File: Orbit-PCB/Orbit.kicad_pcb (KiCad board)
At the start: 2 copper layers, 303.2 x 145.3 mm, 287 parts, among them J1 PJ-3200B-4A, J10 Breakaway_Tabs, J11 PJ-3200B-4A, J12 AVR-ISP-6, J13 Breakaway_Tabs, J14 Breakaway_Tabs, J17 Breakaway_Tabs, J18 Breakaway_Tabs, J19 Breakaway_Tabs, J2 AVR-ISP-6, J20 Breakaway_Tabs, J3 Breakaway_Tabs, J5 Breakaway_Tabs, J6 Breakaway_Tabs, J7 Breakaway_Tabs, J9 Breakaway_Tabs, Q1 2N7002, Q2 2N7002, SW1 SW_Push, SW2 SW_Push, U1 ATmega32U4-MU, U2 PRTR5V0U2X, U3 ATmega32U4-MU, U4 PRTR5V0U2X, Y1 16MHz, Y2 16MHz

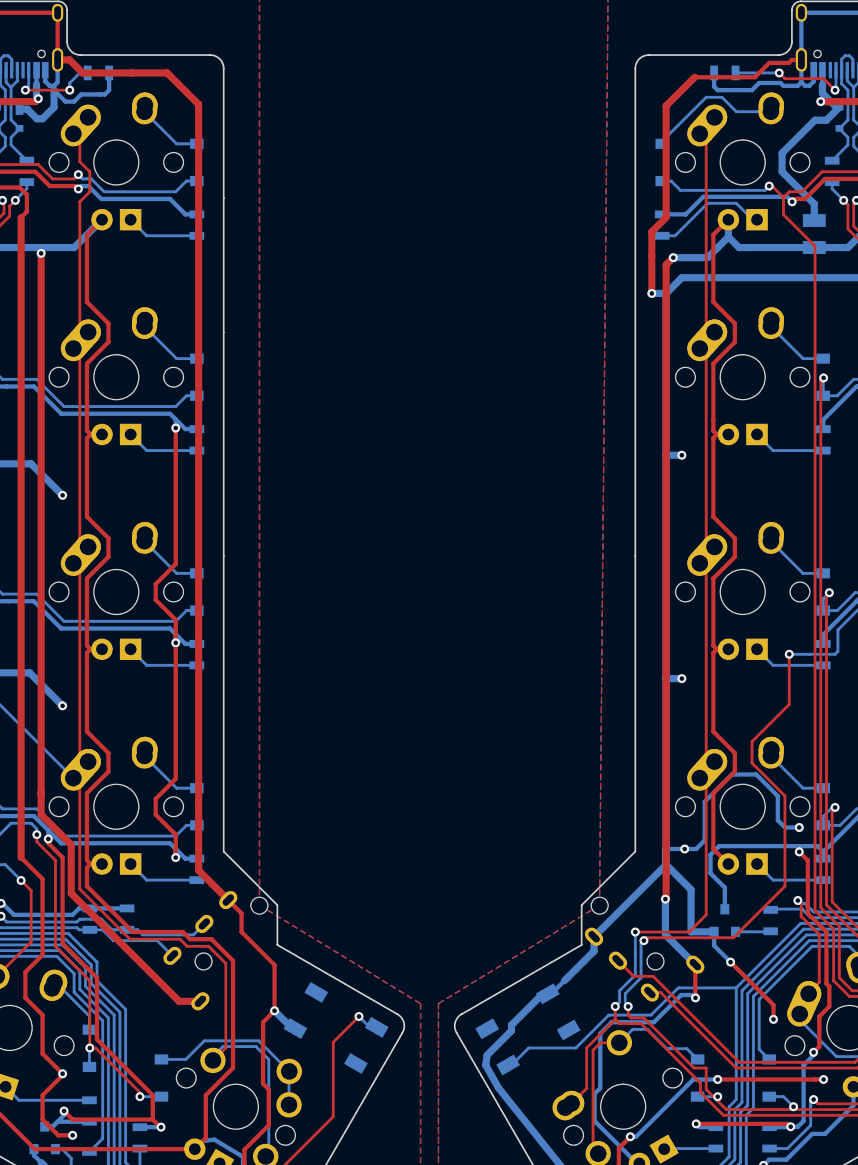
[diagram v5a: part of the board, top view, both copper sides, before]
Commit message: Move TRRS further out
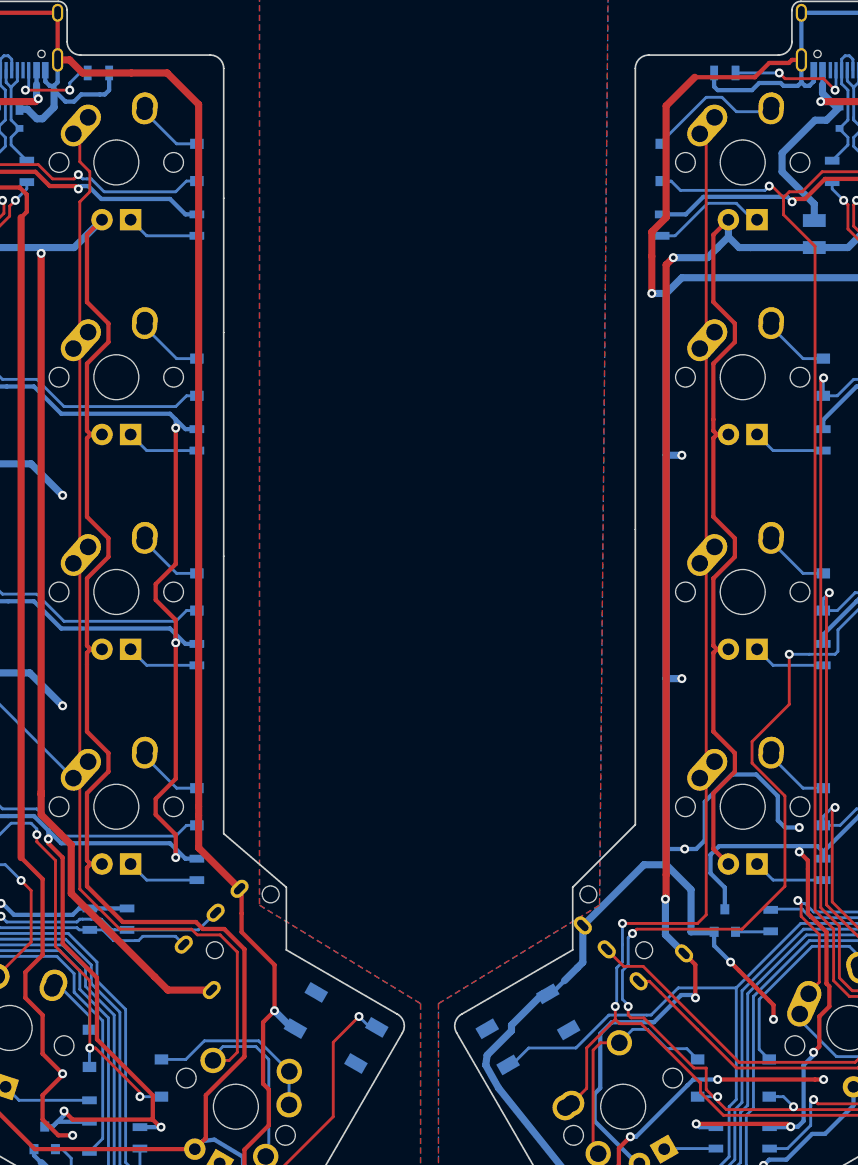
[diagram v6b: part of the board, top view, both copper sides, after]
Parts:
- moved J1 1.41 mm to (168.8, 106.7)
- moved J11 1.41 mm to (194.7, 106.7)
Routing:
- net COL6: track 169.4 -> 172.3 mm
- net +5V: track 1027.8 -> 1030.4 mm
- net SDA-R: track 46.3 -> 47.7 mm
- net SCL-R: track 48.4 -> 49.8 mm
- net ROW4-R: track 240.5 -> 241.6 mm
- net COL0-R: track 152.2 -> 153.4 mm
- net SCL: track 46.3 -> 47.3 mm
- net SDA: track 44.4 -> 45.3 mm
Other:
- outline, holes or cut-outs redrawn

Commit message: Route status LEDs
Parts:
- removed the G*** at (47.6, 117.5)
- removed the G*** at (330.2, 116.7)
- removed the G*** at (33.3, 116.7)
- added D71: LED_3mm, locallib:LED_D3.0mm, F.Cu at (43.7, 121.2)
- added D72: LED_3mm, locallib:LED_D3.0mm, F.Cu at (33.7, 121.2)
- added D73: LED_3mm, locallib:LED_D3.0mm, F.Cu at (319.8, 121.2)
- added D74: LED_3mm, locallib:LED_D3.0mm, F.Cu at (329.8, 121.2)
- added G***: LOGO, locallib:ai-4.8-mask, F.Cu at (49.2, 116.7)
- added R89: 1k, Resistors_SMD:R_0805, B.Cu at (43.7, 116.7)
- added R90: 1k, Resistors_SMD:R_0805, B.Cu at (33.8, 116.7)
- added R91: 1k, Resistors_SMD:R_0805, B.Cu at (319.9, 116.7)
- added R92: 1k, Resistors_SMD:R_0805, B.Cu at (329.8, 116.7)
- D35, D70: value LED_1.8mm -> LED_3mm; footprint LEDs:LED_D3.0mm -> locallib:LED_D3.0mm
- moved R33 9.02 mm to (38.7, 116.7), turned to 0 degrees
- moved R82 8.35 mm to (324.9, 116.7), turned to 180 degrees
- moved G*** 3.55 mm to (314.3, 116.7)
- moved D35 2.24 mm to (38.7, 121.2), turned to 90 degrees
- moved J20 1.59 mm to (323.9, 125.4)
- moved J6 1.59 mm to (39.7, 125.4)
- moved C10 1.34 mm to (226.3, 114.8), turned to 180 degrees
- moved C7 0.92 mm to (132.0, 106.7)
- moved C11 0.56 mm to (237.5, 122.3)
- moved R67 0.41 mm to (240.9, 121.3)
- moved D70 0.37 mm to (324.8, 121.2), turned to 90 degrees
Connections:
- R33 pad 2: LEDIND -> LEDIND-2
- R82 pad 2: LEDIND-R -> LEDIND-2-R
- U1 pad 1: Net-(U1-Pad1) -> LEDIND-3
- U1 pad 25: LEDIND -> LEDIND-1
- U1 pad 41: Net-(U1-Pad41) -> LEDIND-2
- U3 pad 1: Net-(U3-Pad1) -> LEDIND-3-R
- U3 pad 25: LEDIND-R -> LEDIND-1-R
- U3 pad 41: Net-(U3-Pad41) -> LEDIND-2-R
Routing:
- net LEDIND-3-R: track 0.00 -> 174.6 mm, vias 0 -> 4
- net LEDIND-3: track 0.00 -> 139.0 mm, vias 0 -> 4
- net LEDIND-2: track 0.00 -> 131.0 mm, vias 0 -> 4
- net LEDIND-2-R: track 0.00 -> 111.2 mm, vias 0 -> 2
- net LEDIND-1: track 0.00 -> 94.1 mm
- net LEDIND: track 93.5 -> 0.00 mm
- net LEDIND-1-R: track 0.00 -> 91.6 mm
- net LEDIND-R: track 91.1 -> 0.00 mm
- net GNDA: track 1084.5 -> 1095.2 mm, vias 33 -> 35
- net Net-(D35-Pad2): track 10.5 -> 3.59 mm
- net ROW0-R: track 237.8 -> 243.1 mm
- net +5VA: track 983.3 -> 987.3 mm
- net Net-(D71-Pad2): track 0.00 -> 3.61 mm
- net Net-(D73-Pad2): track 0.00 -> 3.59 mm
- net Net-(D72-Pad2): track 0.00 -> 3.57 mm
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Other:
- outline, holes or cut-outs redrawn
- net class POWER: trace_width 0.381 -> 0.635
